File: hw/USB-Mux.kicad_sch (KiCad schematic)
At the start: 63 parts, among them J101 USB-61400416121, J102 USB-676432911, J103 USB-61400416121, J104 USB-676432911, Q101 DTC114EE, Q102 DTC114EE, Q103 DTC114EE, Q104 DTC114EE, U101 TS3USB3000, U102 TS3USB3000, U103 TPS22976, U104 TPS22976, U105 TUSB212, X101 Lightpipe-5x12.7mm-Dome, X102 Lightpipe-5x12.7mm-Dome, X103 Lightpipe-5x12.7mm-Dome, X104 Lightpipe-5x12.7mm-Dome, X105 Lightpipe-5x12.7mm-Dome

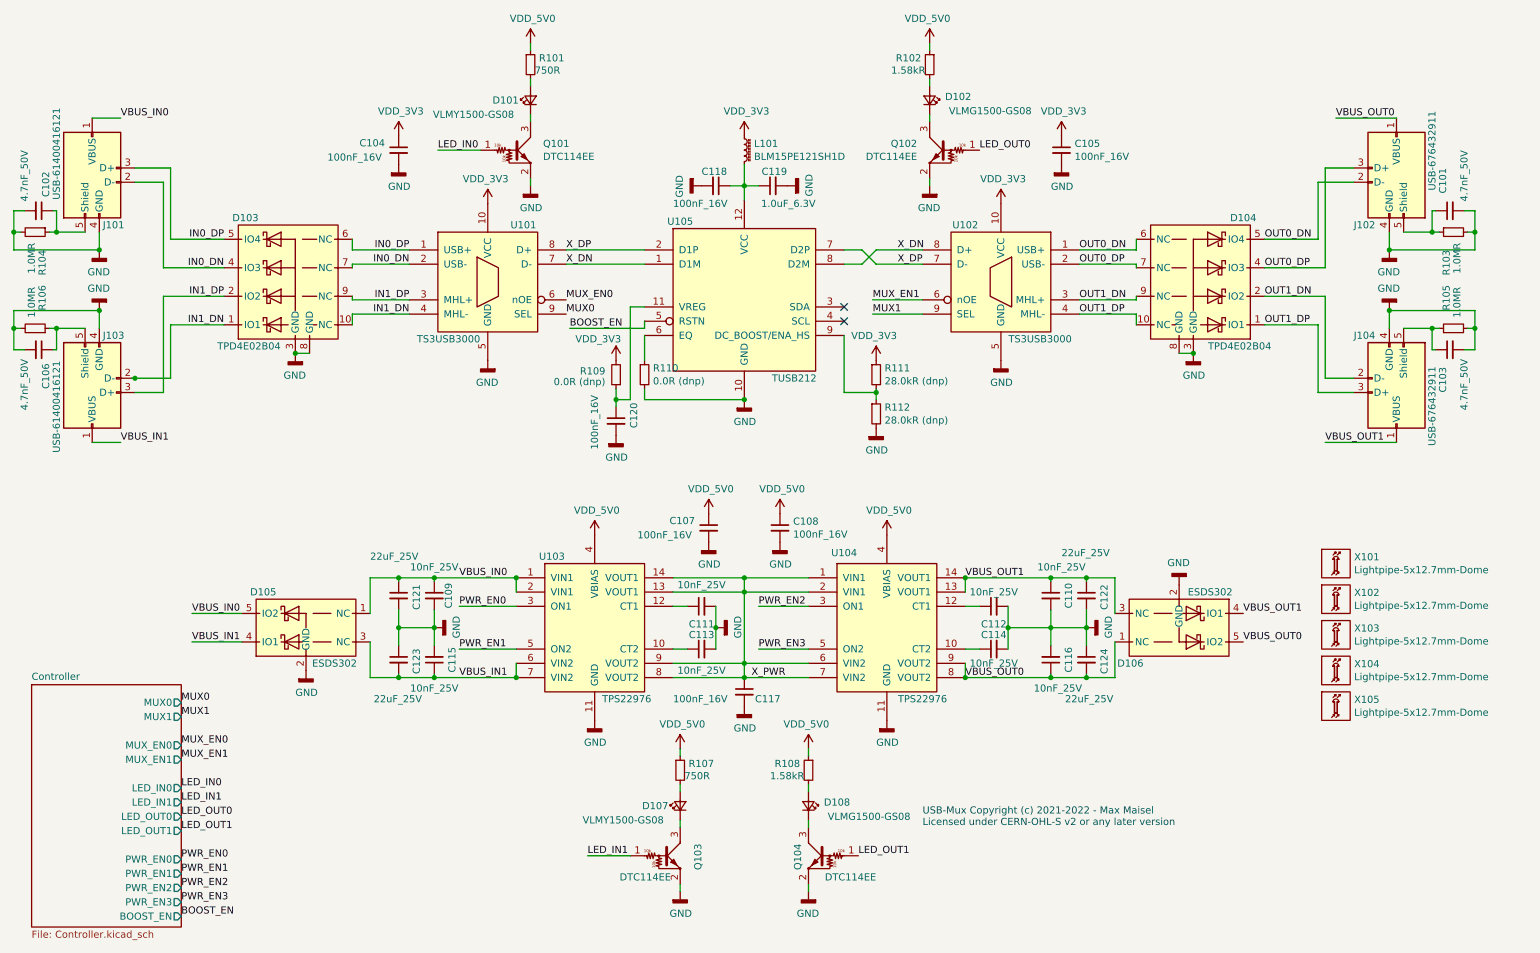
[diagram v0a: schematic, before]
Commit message: Mark dnp components in schematic.
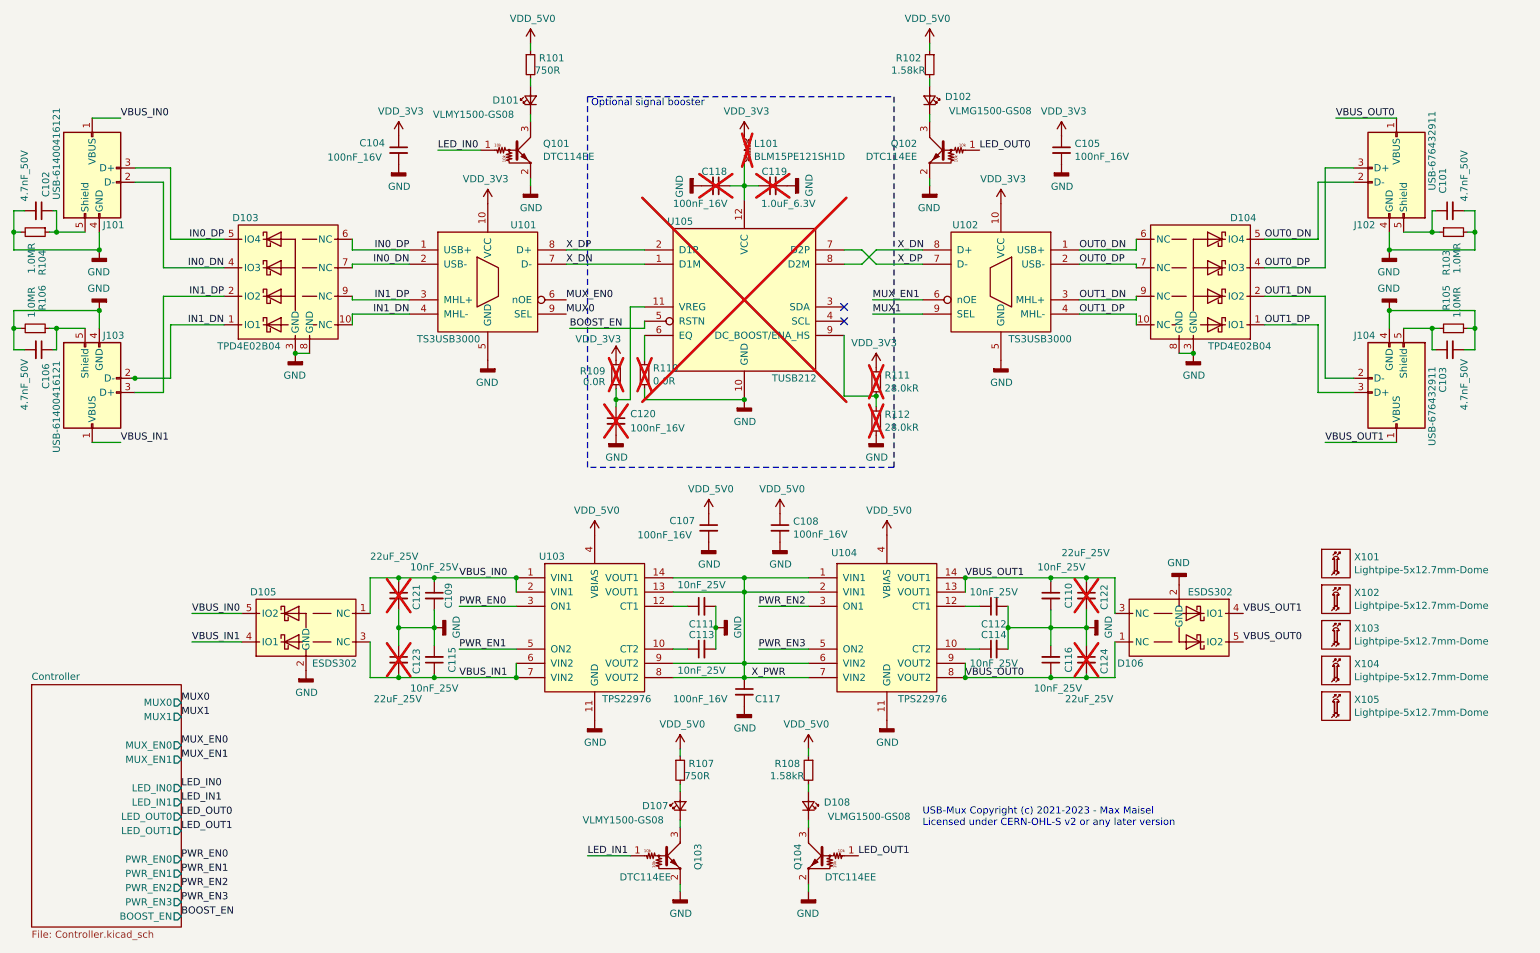
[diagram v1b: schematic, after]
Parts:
- C118, C119, C120, C121, C122, C123, C124, L101, U105: now not fitted
- R109, R110: value 0.0R (dnp) -> 0.0R; now not fitted
- R111, R112: value 28.0kR (dnp) -> 28.0kR; now not fitted
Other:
- note added: "Optional signal booster"
- note added: "USB-Mux Copyright (c) 2021-2023 - Max Maisel Licensed under CERN-OHL-S v2 or any later version"
- note removed: "USB-Mux Copyright (c) 2021-2022 - Max Maisel Licensed under CERN-OHL-S v2 or any later version"
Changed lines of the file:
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@@
   (junction (at 84.455 127) (diameter 0) (color 0 0 0 0)
   )
+  (junction (at 169.545 94.615) (diameter 0) (color 0 0 0 0)
+  )
   (junction (at 193.04 135.89) (diameter 0) (color 0 0 0 0)
   )
@@
   (junction (at 15.875 82.55) (diameter 0) (color 0 0 0 0)
   )
-  (junction (at 169.545 93.98) (diameter 0) (color 0 0 0 0)
-  )
   (junction (at 200.66 127) (diameter 0) (color 0 0 0 0)
   )
@@
     (stroke (width 0) (type default))
   )
+  (wire (pts (xy 169.545 94.615) (xy 169.545 96.52))
+    (stroke (width 0) (type default))
+  )
   (wire (pts (xy 133.35 142.24) (xy 146.05 142.24))
     (stroke (width 0) (type default))
@@
     (stroke (width 0) (type default))
   )
-  (wire (pts (xy 163.83 93.98) (xy 169.545 93.98))
+  (wire (pts (xy 163.83 94.615) (xy 169.545 94.615))
     (stroke (width 0) (type default))
   )
@@
     (stroke (width 0) (type default))
   )
-  (wire (pts (xy 169.545 93.345) (xy 169.545 93.98))
-    (stroke (width 0) (type default))
-  )
   (wire (pts (xy 167.005 71.12) (xy 169.545 68.58))
     (stroke (width 0) (type default))
@@
     (stroke (width 0) (type default))
   )
-  (wire (pts (xy 163.83 83.82) (xy 163.83 93.98))
+  (wire (pts (xy 163.83 83.82) (xy 163.83 94.615))
     (stroke (width 0) (type default))
   )
@@
     (stroke (width 0) (type default))
   )
-  (wire (pts (xy 169.545 93.98) (xy 169.545 95.25))
-    (stroke (width 0) (type default))
-  )
   (wire (pts (xy 79.375 144.78) (xy 84.455 144.78))
     (stroke (width 0) (type default))
@@
     (stroke (width 0) (type default))
   )
-  (text "USB-Mux Copyright (c) 2021-2022 - Max Maisel\nLicensed under CERN-OHL-S v2 or any later version"
+  (rectangle (start 118.11 41.275) (end 172.72 107.315)
+    (stroke (width 0) (type dash))
+    (fill (type none))
+  )
+  (text "Optional signal booster" (at 118.745 43.18 0)
+    (effects (font (size 1.27 1.27)) (justify left bottom))
+  )
+  (text "USB-Mux Copyright (c) 2021-2023 - Max Maisel\nLicensed under CERN-OHL-S v2 or any later version"
     (at 177.8 171.45 0)
     (effects (font (size 1.27 1.27)) (justify left bottom))
@@
   )
   (symbol (lib_id "USB-Mux:100nF_16V") (at 123.19 99.06 0) (unit 1)
-    (in_bom yes) (on_board yes) (dnp no)
-    (property "Reference" "C120" (at 126.365 100.33 90)
+    (in_bom yes) (on_board yes) (dnp yes)
+    (property "Reference" "C120" (at 125.73 97.79 0)
       (effects (font (size 1.27 1.27)) (justify left))
     )
-    (property "Value" "100nF_16V" (at 119.38 104.14 90)
+    (property "Value" "100nF_16V" (at 125.73 100.33 0)
       (effects (font (size 1.27 1.27)) (justify left))
     )
@@
   )
   (symbol (lib_id "USB-Mux:0.0R") (at 123.19 90.805 180) (unit 1)
-    (in_bom yes) (on_board yes) (dnp no)
+    (in_bom yes) (on_board yes) (dnp yes)
     (property "Reference" "R109" (at 121.285 90.17 0)
       (effects (font (size 1.27 1.27)) (justify left))
     )
-    (property "Value" "0.0R (dnp)" (at 121.285 92.075 0)
+    (property "Value" "0.0R" (at 121.285 92.075 0)
       (effects (font (size 1.27 1.27)) (justify left))
     )
@@
   )
   (symbol (lib_id "USB-Mux:BLM15PE121SH1D") (at 146.05 50.8 0) (unit 1)
-    (in_bom yes) (on_board yes) (dnp no)
+    (in_bom yes) (on_board yes) (dnp yes)
     (property "Reference" "L101" (at 147.7772 49.6316 0)
       (effects (font (size 1.27 1.27)) (justify left))
@@
   )
   (symbol (lib_id "USB-Mux:0.0R") (at 128.27 90.805 0) (unit 1)
-    (in_bom yes) (on_board yes) (dnp no)
+    (in_bom yes) (on_board yes) (dnp yes)
     (property "Reference" "R110" (at 129.7686 89.6366 0)
       (effects (font (size 1.27 1.27)) (justify left))
     )
-    (property "Value" "0.0R (dnp)" (at 129.7686 91.948 0)
+    (property "Value" "0.0R" (at 129.7686 91.948 0)
       (effects (font (size 1.27 1.27)) (justify left))
     )
@@
   )
   (symbol (lib_id "USB-Mux:TUSB212") (at 146.05 77.47 0) (unit 1)
-    (in_bom yes) (on_board yes) (dnp no)
+    (in_bom yes) (on_board yes) (dnp yes)
     (property "Reference" "U105" (at 134.62 63.5 0)
       (effects (font (size 1.27 1.27)))
@@
   )
   (symbol (lib_id "USB-Mux:22uF_25V") (at 84.455 130.175 0) (unit 1)
-    (in_bom yes) (on_board yes) (dnp no)
+    (in_bom yes) (on_board yes) (dnp yes)
     (property "Reference" "C121" (at 87.63 132.715 90)
       (effects (font (size 1.27 1.27)) (justify left))
@@
   )
   (symbol (lib_id "USB-Mux:22uF_25V") (at 84.455 141.605 0) (unit 1)
-    (in_bom yes) (on_board yes) (dnp no)
+    (in_bom yes) (on_board yes) (dnp yes)
     (property "Reference" "C123" (at 87.63 144.145 90)
       (effects (font (size 1.27 1.27)) (justify left))
@@
   )
   (symbol (lib_id "USB-Mux:22uF_25V") (at 207.01 130.175 0) (unit 1)
-    (in_bom yes) (on_board yes) (dnp no)
+    (in_bom yes) (on_board yes) (dnp yes)
     (property "Reference" "C122" (at 210.185 132.715 90)
       (effects (font (size 1.27 1.27)) (justify left))
@@
   )
   (symbol (lib_id "USB-Mux:22uF_25V") (at 207.01 141.605 0) (unit 1)
-    (in_bom yes) (on_board yes) (dnp no)
+    (in_bom yes) (on_board yes) (dnp yes)
     (property "Reference" "C124" (at 210.185 144.145 90)
       (effects (font (size 1.27 1.27)) (justify left))
@@
     )
   )
-  (symbol (lib_id "USB-Mux:28.0kR") (at 169.545 90.805 0) (unit 1)
-    (in_bom yes) (on_board yes) (dnp no)
-    (property "Reference" "R111" (at 171.0436 89.6366 0)
+  (symbol (lib_id "USB-Mux:28.0kR") (at 169.545 92.075 0) (unit 1)
+    (in_bom yes) (on_board yes) (dnp yes)
+    (property "Reference" "R111" (at 171.0436 90.9066 0)
       (effects (font (size 1.27 1.27)) (justify left))
     )
-    (property "Value" "28.0kR (dnp)" (at 171.0436 91.948 0)
+    (property "Value" "28.0kR" (at 171.0436 93.218 0)
       (effects (font (size 1.27 1.27)) (justify left))
     )
-    (property "Footprint" "USB-Mux:R_0402" (at 167.767 92.837 0)
+    (property "Footprint" "USB-Mux:R_0402" (at 167.767 94.107 0)
       (effects (font (size 1.27 1.27)) hide)
     )
-    (property "Datasheet" "667-ERJ-2RKF2802X" (at 170.307 90.297 0)
+    (property "Datasheet" "667-ERJ-2RKF2802X" (at 170.307 91.567 0)
       (effects (font (size 1.27 1.27)) hide)
     )
-    (property "mouser#" "667-ERJ-2RKF2802X" (at 172.847 87.757 0)
+    (property "mouser#" "667-ERJ-2RKF2802X" (at 172.847 89.027 0)
       (effects (font (size 1.524 1.524)) hide)
     )
@@
     )
   )
-  (symbol (lib_id "USB-Mux:28.0kR") (at 169.545 97.79 0) (unit 1)
-    (in_bom yes) (on_board yes) (dnp no)
-    (property "Reference" "R112" (at 171.0436 96.6216 0)
+  (symbol (lib_id "USB-Mux:28.0kR") (at 169.545 99.06 0) (unit 1)
+    (in_bom yes) (on_board yes) (dnp yes)
+    (property "Reference" "R112" (at 171.0436 97.8916 0)
       (effects (font (size 1.27 1.27)) (justify left))
     )
-    (property "Value" "28.0kR (dnp)" (at 171.0436 98.933 0)
+    (property "Value" "28.0kR" (at 171.0436 100.203 0)
       (effects (font (size 1.27 1.27)) (justify left))
     )
-    (property "Footprint" "USB-Mux:R_0402" (at 167.767 99.822 0)
+    (property "Footprint" "USB-Mux:R_0402" (at 167.767 101.092 0)
       (effects (font (size 1.27 1.27)) hide)
     )
-    (property "Datasheet" "667-ERJ-2RKF2802X" (at 170.307 97.282 0)
+    (property "Datasheet" "667-ERJ-2RKF2802X" (at 170.307 98.552 0)
       (effects (font (size 1.27 1.27)) hide)
     )
-    (property "mouser#" "667-ERJ-2RKF2802X" (at 172.847 94.742 0)
+    (property "mouser#" "667-ERJ-2RKF2802X" (at 172.847 96.012 0)
       (effects (font (size 1.524 1.524)) hide)
     )
@@
   )
   (symbol (lib_id "USB-Mux:100nF_16V") (at 140.97 57.15 270) (unit 1)
-    (in_bom yes) (on_board yes) (dnp no)
+    (in_bom yes) (on_board yes) (dnp yes)
     (property "Reference" "C118" (at 138.43 54.61 90)
       (effects (font (size 1.27 1.27)) (justify left))
@@
   )
   (symbol (lib_id "USB-Mux:1.0uF_6.3V") (at 151.13 57.15 90) (unit 1)
-    (in_bom yes) (on_board yes) (dnp no)
+    (in_bom yes) (on_board yes) (dnp yes)
     (property "Reference" "C119" (at 153.67 54.61 90)
       (effects (font (size 1.27 1.27)) (justify left))
@@
     )
   )
-  (symbol (lib_id "USB-Mux:VDD_3V3") (at 169.545 88.265 0) (mirror y) (unit 1)
+  (symbol (lib_id "USB-Mux:VDD_3V3") (at 169.545 89.535 0) (mirror y) (unit 1)
     (in_bom yes) (on_board yes) (dnp no)
-    (property "Reference" "#PWR0139" (at 169.545 92.075 0)
+    (property "Reference" "#PWR0139" (at 169.545 93.345 0)
       (effects (font (size 1.27 1.27)) hide)
     )
-    (property "Value" "VDD_3V3" (at 169.164 83.8708 0)
+    (property "Value" "VDD_3V3" (at 169.164 85.1408 0)
       (effects (font (size 1.27 1.27)))
     )
-    (property "Footprint" "" (at 169.545 88.265 0)
+    (property "Footprint" "" (at 169.545 89.535 0)
       (effects (font (size 1.27 1.27)) hide)
     )
-    (property "Datasheet" "" (at 169.545 88.265 0)
+    (property "Datasheet" "" (at 169.545 89.535 0)
       (effects (font (size 1.27 1.27)) hide)
     )
@@
     )
   )
-  (symbol (lib_id "USB-Mux:GND") (at 169.545 100.33 0) (unit 1)
+  (symbol (lib_id "USB-Mux:GND") (at 169.545 101.6 0) (unit 1)
     (in_bom yes) (on_board yes) (dnp no)
-    (property "Reference" "#PWR0141" (at 169.545 106.68 0)
+    (property "Reference" "#PWR0141" (at 169.545 107.95 0)
       (effects (font (size 1.27 1.27)) hide)
     )
-    (property "Value" "GND" (at 169.6466 104.267 0)
+    (property "Value" "GND" (at 169.6466 105.537 0)
       (effects (font (size 1.27 1.27)))
     )
-    (property "Footprint" "" (at 169.545 100.33 0)
+    (property "Footprint" "" (at 169.545 101.6 0)
       (effects (font (size 1.27 1.27)) hide)
     )
-    (property "Datasheet" "~" (at 169.545 100.33 0)
+    (property "Datasheet" "~" (at 169.545 101.6 0)
       (effects (font (size 1.27 1.27)) hide)
     )

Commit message: Add some missing component ordering numbers.
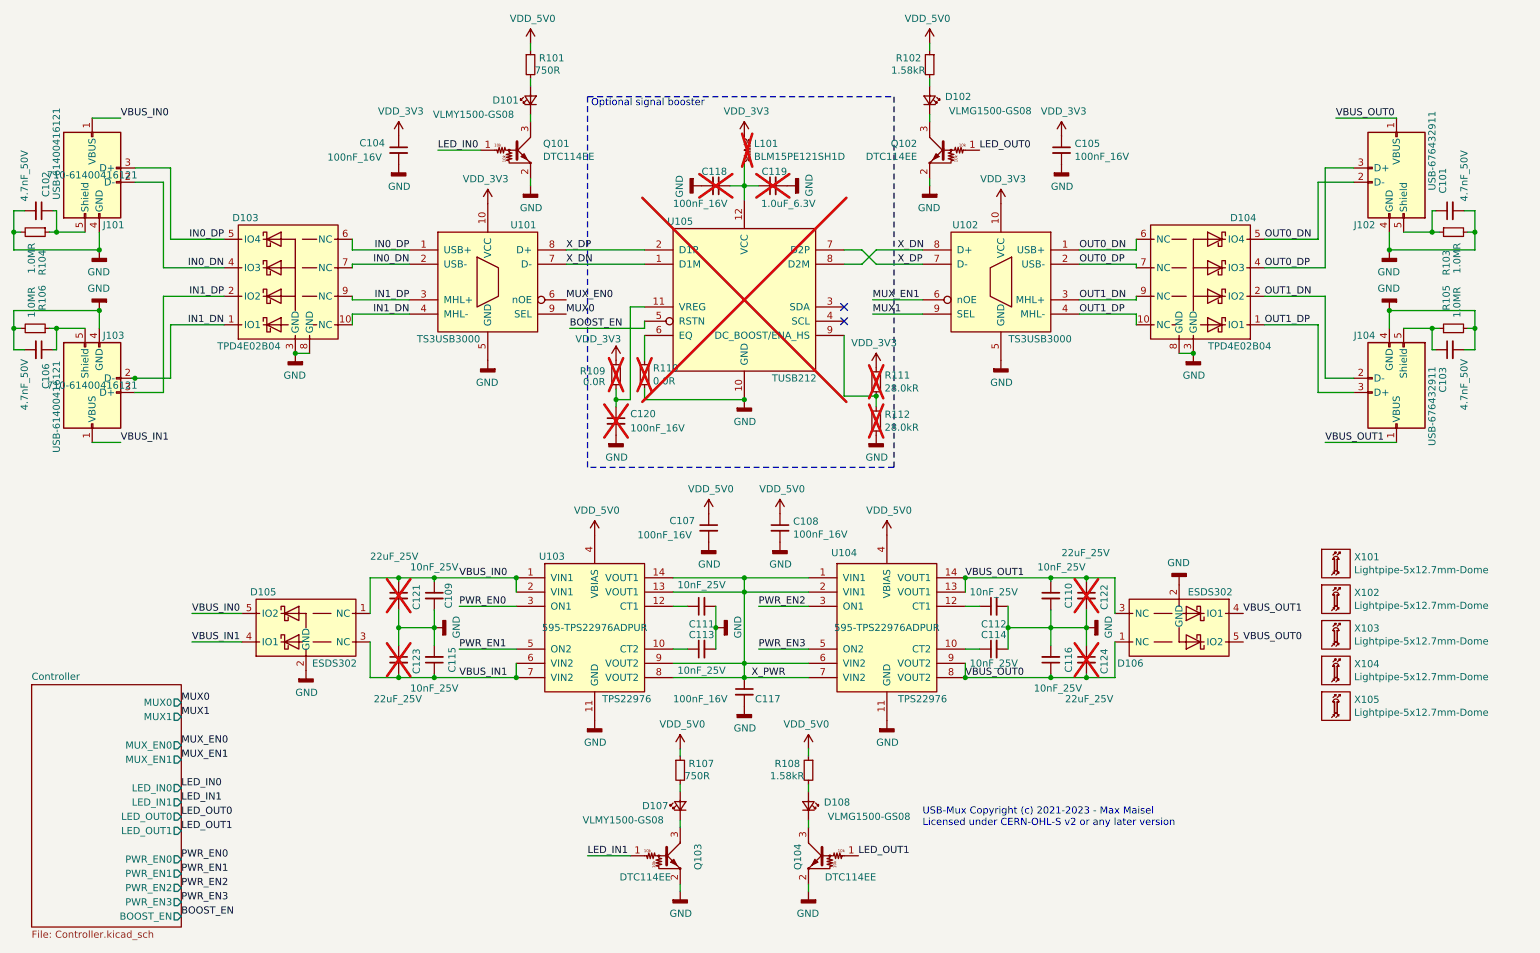
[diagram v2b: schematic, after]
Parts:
- J101, J103: mouser# (none) -> 710-61400416121
- U103, U104: mouser# (none) -> 595-TPS22976ADPUR
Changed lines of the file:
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@@
       (effects (font (size 1.27 1.27)) hide)
+    )
+    (property "mouser#" "710-61400416121 " (at 29.845 55.245 0)
+      (effects (font (size 1.27 1.27)))
     )
     (pin "1")
@@
       (effects (font (size 1.27 1.27)) hide)
     )
-    (property "Datasheet" "" (at 109.22 144.78 0)
-      (effects (font (size 1.27 1.27)) hide)
+    (property "Datasheet" "https://www.ti.com/lit/ds/symlink/tps22976.pdf" (at 109.22 144.78 0)
+      (effects (font (size 1.27 1.27)) hide)
+    )
+    (property "mouser#" "595-TPS22976ADPUR" (at 119.38 135.89 0)
+      (effects (font (size 1.27 1.27)))
     )
     (pin "1")
@@
       (effects (font (size 1.27 1.27)) hide)
     )
-    (property "Datasheet" "" (at 161.29 144.78 0)
-      (effects (font (size 1.27 1.27)) hide)
+    (property "Datasheet" "https://www.ti.com/lit/ds/symlink/tps22976.pdf" (at 161.29 144.78 0)
+      (effects (font (size 1.27 1.27)) hide)
+    )
+    (property "mouser#" "595-TPS22976ADPUR" (at 171.45 135.89 0)
+      (effects (font (size 1.27 1.27)))
     )
     (pin "1")
@@
       (effects (font (size 1.27 1.27)) hide)
     )
-    (pin "1")
+    (property "mouser#" "710-61400416121 " (at 29.845 92.71 0)
+      (effects (font (size 1.27 1.27)))
+    )
+    (pin "1")
